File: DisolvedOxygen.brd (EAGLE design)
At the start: 95 x 25 mm, 28 parts, among them J1 2X6-HEADERS, U2 MPL3115A2LGA8, U3 M24C02-WMN6TP

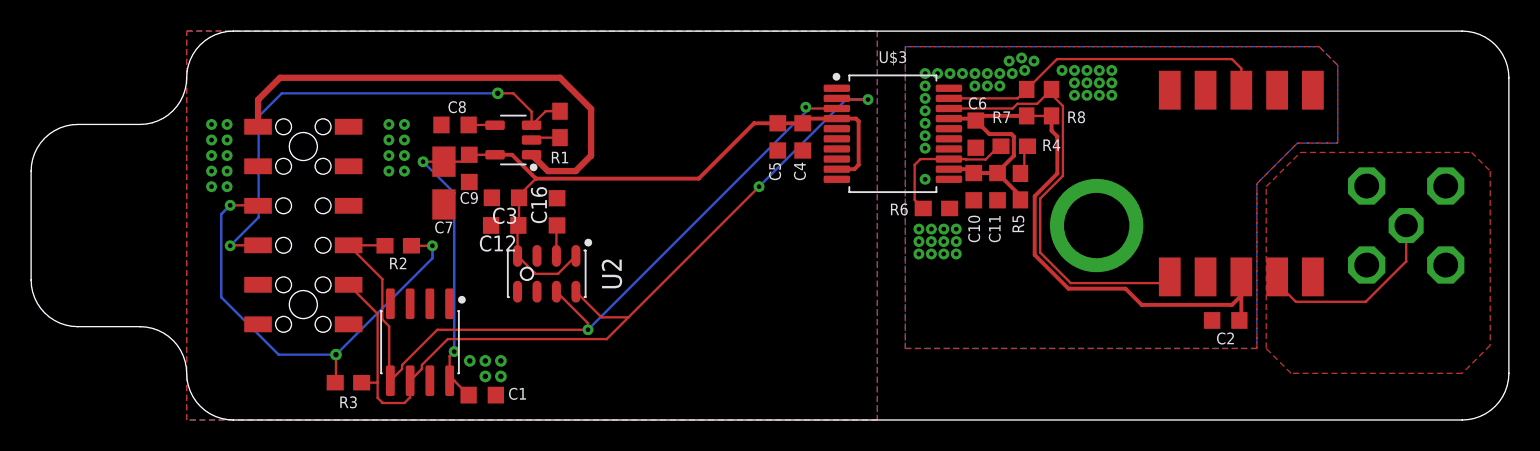
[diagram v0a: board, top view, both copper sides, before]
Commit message: Quadfurcated modules into individual files, migrated to new footprint, added module tags to tabs, moved Weather programming header.
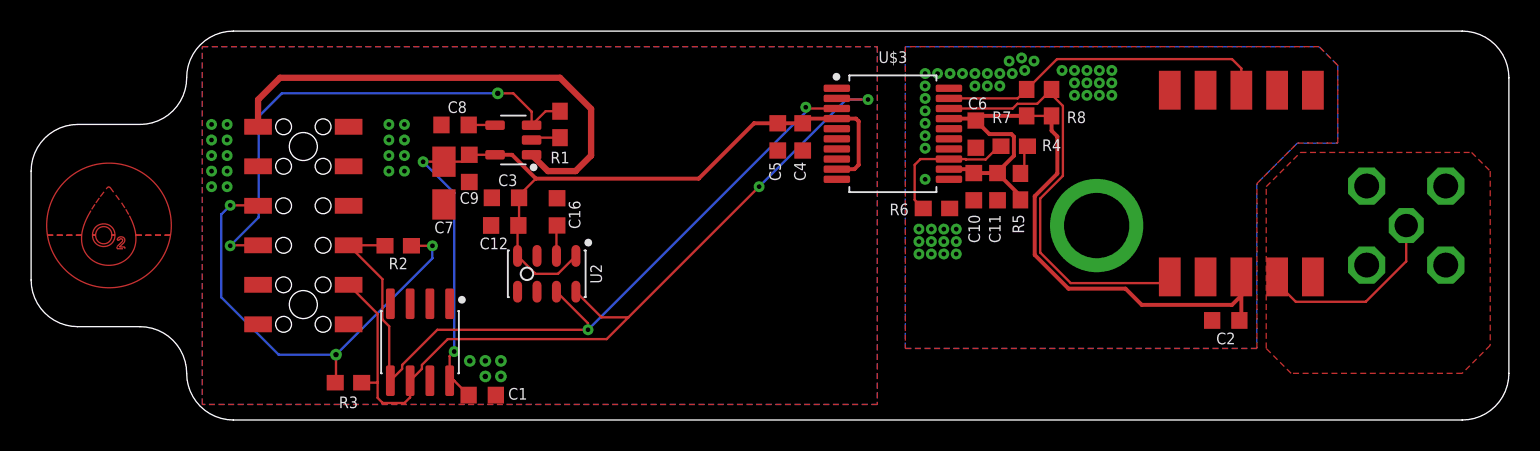
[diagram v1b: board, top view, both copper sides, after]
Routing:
- added copper zone on layer 1, net GND1
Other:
- board text added: "THIS SIDE DOWN"
